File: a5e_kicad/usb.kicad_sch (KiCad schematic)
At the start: 7 parts, among them U1801 USB3320C-EZK

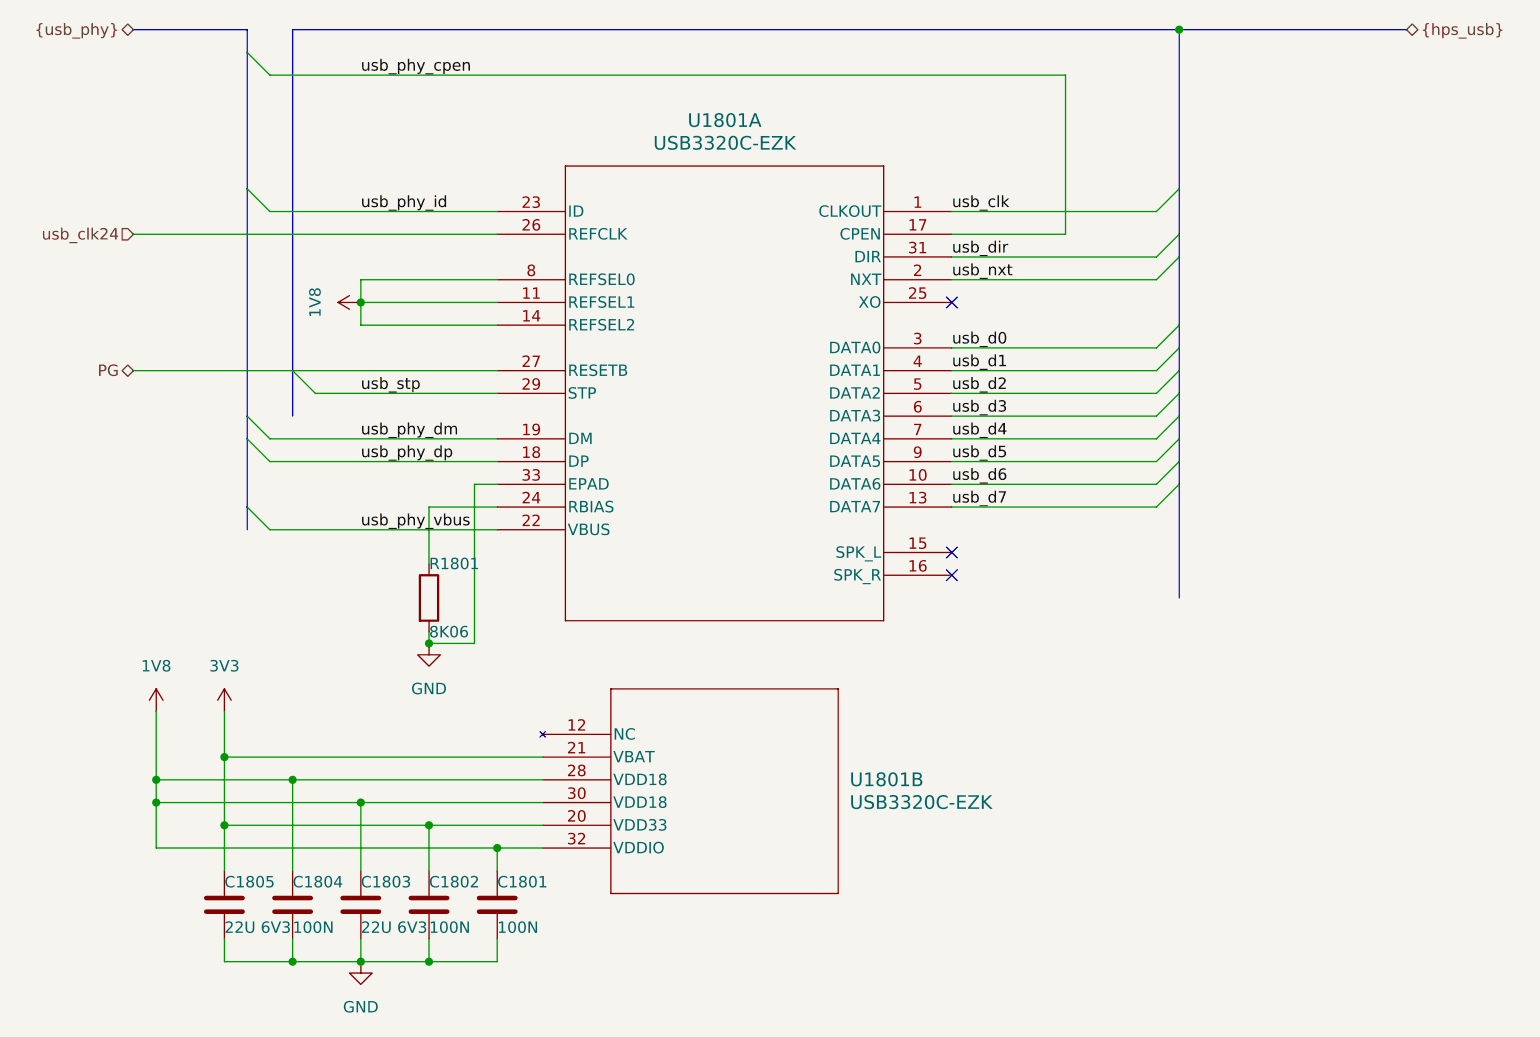
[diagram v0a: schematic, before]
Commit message: add vias to lppdr balls
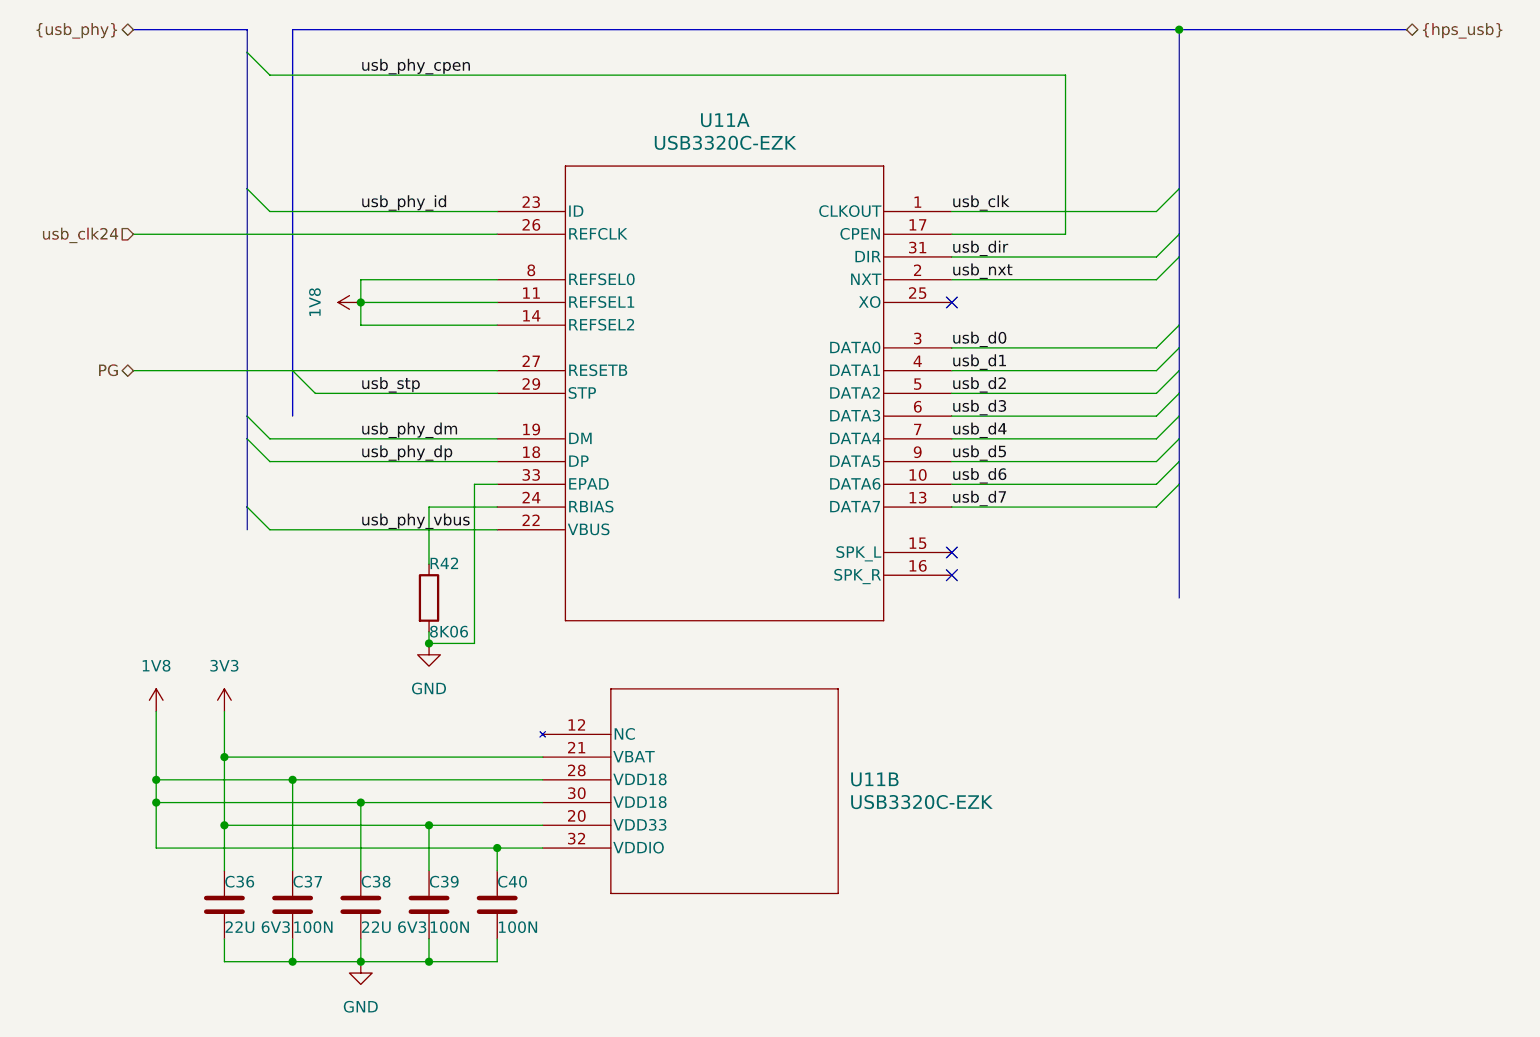
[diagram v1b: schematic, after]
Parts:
- renumbered C1805 to C36, C1804 to C37, C1803 to C38, C1802 to C39, C1801 to C40, R1801 to R42, U1801 to U11
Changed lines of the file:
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@@
 		(dnp no)
 		(fields_autoplaced yes)
-		(property "Reference" "U1801"
+		(property "Reference" "U11"
 			(at 109.22 48.26 0)
 			(show_name no)
@@
 			(project "agilex_3_soc"
 				(path "/a5b98d95-6877-4284-904f-d04e32723ae0/441b8b06-7331-4f52-9ed6-a8466553125b"
-					(reference "U1801")
+					(reference "U11")
 					(unit 1)
 				)
@@
 		(in_pos_files yes)
 		(dnp no)
-		(property "Reference" "C1803"
+		(property "Reference" "C38"
 			(at 68.58 133.35 0)
 			(show_name no)
@@
 			(project "agilex_3_soc"
 				(path "/a5b98d95-6877-4284-904f-d04e32723ae0/441b8b06-7331-4f52-9ed6-a8466553125b"
-					(reference "C1803")
+					(reference "C38")
 					(unit 1)
 				)
@@
 		(in_pos_files yes)
 		(dnp no)
-		(property "Reference" "#PWR01803"
+		(property "Reference" "#PWR088"
 			(at 45.72 118.11 0)
 			(hide yes)
@@
 			(project "agilex_3_soc"
 				(path "/a5b98d95-6877-4284-904f-d04e32723ae0/441b8b06-7331-4f52-9ed6-a8466553125b"
-					(reference "#PWR01803")
+					(reference "#PWR088")
 					(unit 1)
 				)
@@
 		(in_pos_files yes)
 		(dnp no)
-		(property "Reference" "C1801"
+		(property "Reference" "C40"
 			(at 83.82 133.35 0)
 			(show_name no)
@@
 			(project "agilex_3_soc"
 				(path "/a5b98d95-6877-4284-904f-d04e32723ae0/441b8b06-7331-4f52-9ed6-a8466553125b"
-					(reference "C1801")
+					(reference "C40")
 					(unit 1)
 				)
@@
 		(in_pos_files yes)
 		(dnp no)
-		(property "Reference" "C1802"
+		(property "Reference" "C39"
 			(at 76.2 133.35 0)
 			(show_name no)
@@
 			(project "agilex_3_soc"
 				(path "/a5b98d95-6877-4284-904f-d04e32723ae0/441b8b06-7331-4f52-9ed6-a8466553125b"
-					(reference "C1802")
+					(reference "C39")
 					(unit 1)
 				)
@@
 		(in_pos_files yes)
 		(dnp no)
-		(property "Reference" "R1801"
+		(property "Reference" "R42"
 			(at 76.2 97.79 0)
 			(show_name no)
@@
 			(project "agilex_3_soc"
 				(path "/a5b98d95-6877-4284-904f-d04e32723ae0/441b8b06-7331-4f52-9ed6-a8466553125b"
-					(reference "R1801")
+					(reference "R42")
 					(unit 1)
 				)
@@
 		(in_pos_files yes)
 		(dnp no)
-		(property "Reference" "C1805"
+		(property "Reference" "C36"
 			(at 53.34 133.35 0)
 			(show_name no)
@@
 			(project "agilex_3_soc"
 				(path "/a5b98d95-6877-4284-904f-d04e32723ae0/441b8b06-7331-4f52-9ed6-a8466553125b"
-					(reference "C1805")
+					(reference "C36")
 					(unit 1)
 				)
@@
 		(in_pos_files yes)
 		(dnp no)
-		(property "Reference" "#PWR01801"
+		(property "Reference" "#PWR092"
 			(at 76.2 113.03 0)
 			(hide yes)
@@
 			(project "agilex_3_soc"
 				(path "/a5b98d95-6877-4284-904f-d04e32723ae0/441b8b06-7331-4f52-9ed6-a8466553125b"
-					(reference "#PWR01801")
+					(reference "#PWR092")
 					(unit 1)
 				)
@@
 		(dnp no)
 		(fields_autoplaced yes)
-		(property "Reference" "U1801"
+		(property "Reference" "U11"
 			(at 123.19 121.9199 0)
 			(show_name no)
@@
 			(project "agilex_3_soc"
 				(path "/a5b98d95-6877-4284-904f-d04e32723ae0/441b8b06-7331-4f52-9ed6-a8466553125b"
-					(reference "U1801")
+					(reference "U11")
 					(unit 2)
 				)
@@
 		(in_pos_files yes)
 		(dnp no)
-		(property "Reference" "#PWR01802"
+		(property "Reference" "#PWR090"
 			(at 72.39 68.58 0)
 			(hide yes)
@@
 			(project "agilex_3_soc"
 				(path "/a5b98d95-6877-4284-904f-d04e32723ae0/441b8b06-7331-4f52-9ed6-a8466553125b"
-					(reference "#PWR01802")
+					(reference "#PWR090")
 					(unit 1)
 				)
@@
 		(in_pos_files yes)
 		(dnp no)
-		(property "Reference" "#PWR01805"
+		(property "Reference" "#PWR091"
 			(at 68.58 148.59 0)
 			(hide yes)
@@
 			(project "agilex_3_soc"
 				(path "/a5b98d95-6877-4284-904f-d04e32723ae0/441b8b06-7331-4f52-9ed6-a8466553125b"
-					(reference "#PWR01805")
+					(reference "#PWR091")
 					(unit 1)
 				)
@@
 		(in_pos_files yes)
 		(dnp no)
-		(property "Reference" "C1804"
+		(property "Reference" "C37"
 			(at 60.96 133.35 0)
 			(show_name no)
@@
 			(project "agilex_3_soc"
 				(path "/a5b98d95-6877-4284-904f-d04e32723ae0/441b8b06-7331-4f52-9ed6-a8466553125b"
-					(reference "C1804")
+					(reference "C37")
 					(unit 1)
 				)
@@
 		(in_pos_files yes)
 		(dnp no)
-		(property "Reference" "#PWR01804"
+		(property "Reference" "#PWR089"
 			(at 53.34 118.11 0)
 			(hide yes)
@@
 			(project "agilex_3_soc"
 				(path "/a5b98d95-6877-4284-904f-d04e32723ae0/441b8b06-7331-4f52-9ed6-a8466553125b"
-					(reference "#PWR01804")
-					(unit 1)
-				)
+					(reference "#PWR089")
+					(unit 1)
+				)
